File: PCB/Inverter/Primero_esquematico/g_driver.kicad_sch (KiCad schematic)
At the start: 31 parts, among them SW1 SW_Push, U14 SN74LVC1G08DCKR, U3 FS950R08A6P2BBPSA1

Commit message: Correcciones incompletas e instalaciones de un par de extensiones copadas
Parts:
- removed R29, R30, R31, R32, R33, R49, R50, R51, R52, R53, R69, R70, R71: 220k, symbol Device:R
- removed R34, R54: 6k8, symbol Device:R
- added R75, R76, R77, R84, R89, R90, R91, R93: 220k, symbol Device:R
- added R79: 6k8, symbol Device:R
- added TH1: ND03N00103K--, Capacitor_THT:C_Disc_D3.4mm_W2.1mm_P2.50mm, symbol Device:Thermistor_NTC
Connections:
- net GDsupply3/ISO_GND: now also R72.1, R74.2; no longer R74.1
- net GDsupply3/S_HV: now also R77.1; no longer R73.1, R74.2
- net GDsupply4/ISO_GND: now also TH1.1
- net GDsupply4/S_HV: now also TH1.2
- net GDsupply5/ISO_GND: now also R79.2, R84.1
- net GDsupply5/S_HV: now also R93.1
- net GND_DC: now also R74.1, R79.1
- new net: R89.1, R90.1
- new net: R84.2, R89.2
- new net: R73.1, R75.1
- new net: R90.2, R91.2
- new net: R75.2, R76.2
- new net: R76.1, R77.2
- new net: R91.1, R93.2
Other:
- removed sheet LogicSupply
- moved on the sheet: C67, C68, D84, D85, D86, R103, R104, R123, R124, R125, SW1, U14

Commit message: Termine el circuito de corriente
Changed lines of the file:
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@@
-	(wire
-		(pts
-			(xy 349.25 135.89) (xy 332.74 135.89)
-		)
-		(stroke
-			(width 0)
-			(type default)
-		)
-	)
 	(wire
 		(pts
@@
 	(wire
 		(pts
-			(xy 316.23 114.3) (xy 316.23 116.84)
-		)
-		(stroke
-			(width 0)
-			(type default)
-		)
-	)
-	(wire
-		(pts
 			(xy 223.52 144.78) (xy 226.06 144.78)
 		)
@@
 	(wire
 		(pts
-			(xy 332.74 135.89) (xy 332.74 114.3)
-		)
-		(stroke
-			(width 0)
-			(type default)
-		)
-	)
-	(wire
-		(pts
 			(xy 149.86 80.01) (xy 143.51 80.01)
 		)
@@
 	(wire
 		(pts
-			(xy 341.63 114.3) (xy 347.98 114.3)
-		)
-		(stroke
-			(width 0)
-			(type default)
-		)
-	)
-	(wire
-		(pts
 			(xy 207.01 93.98) (xy 199.39 93.98)
 		)
@@
 		)
 		(stroke
-			(width 0)
-			(type default)
-		)
-	)
-	(wire
-		(pts
-			(xy 332.74 114.3) (xy 334.01 114.3)
-		)
-		(stroke

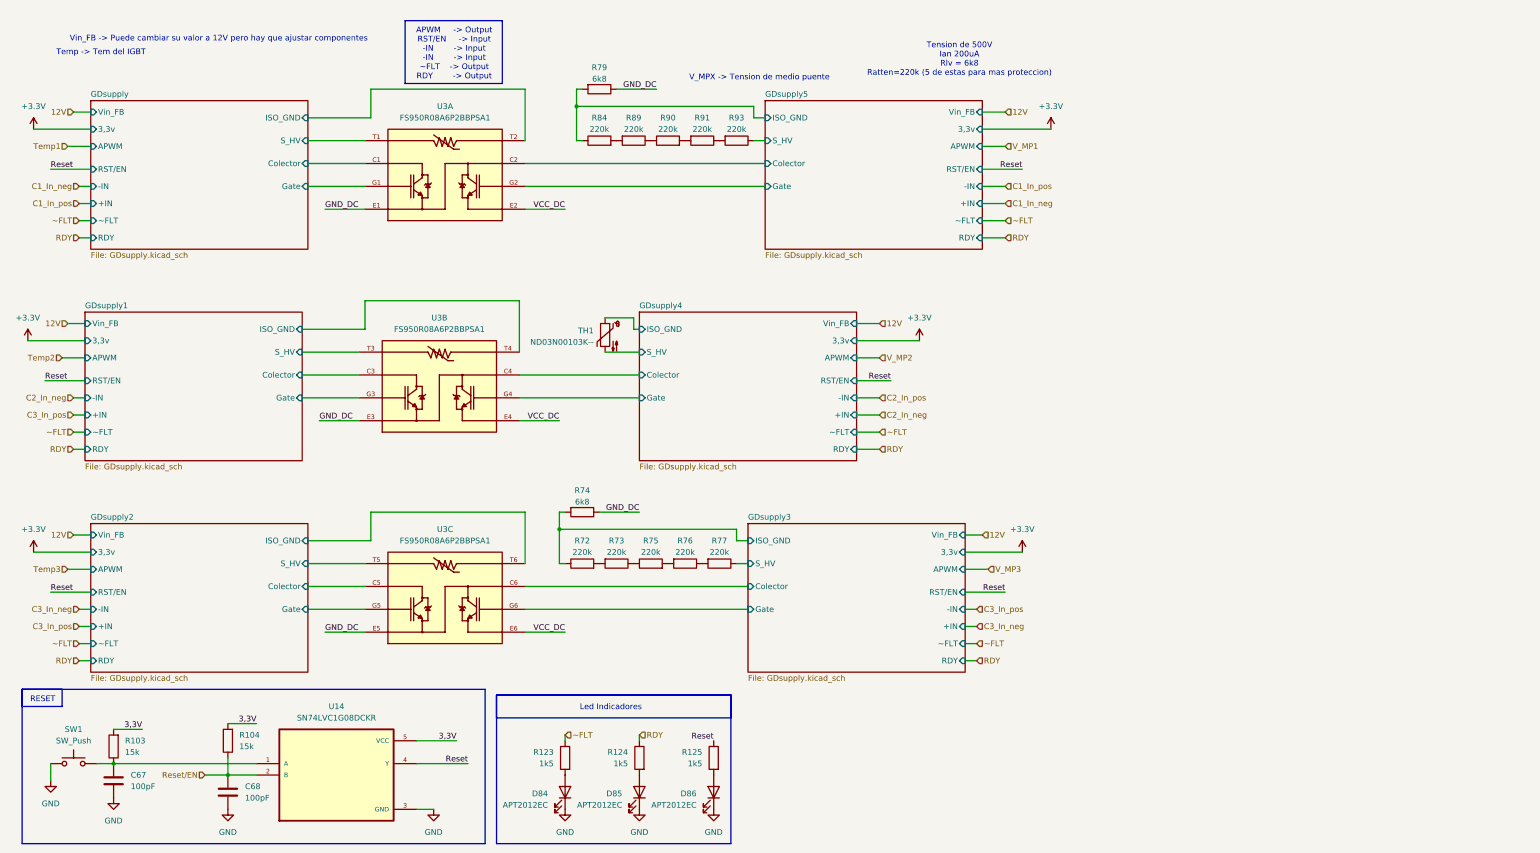
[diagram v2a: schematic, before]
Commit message: Coloque filtros y sensores
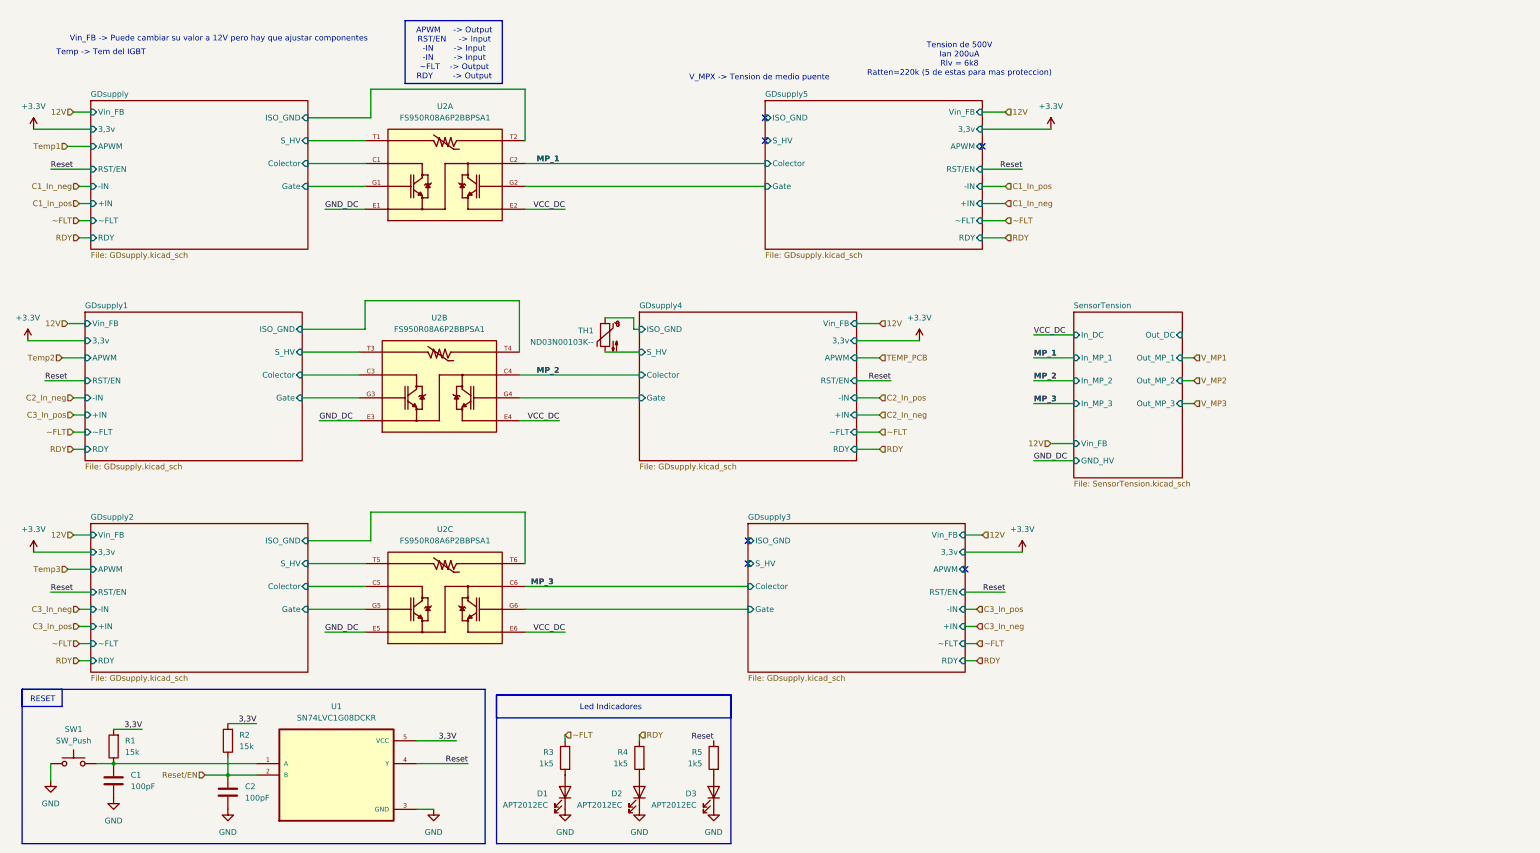
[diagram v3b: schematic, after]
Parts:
- removed R72, R73, R75, R76, R77, R84, R89, R90, R91, R93: 220k, symbol Device:R
- removed R74, R79: 6k8, symbol Device:R
- U1: renamed from U14; footprint SN74LVC1G08DCKR:SOT65P210X110-5N -> Snapeda:SOT65P210X110-5N
- U2: renamed from U3; footprint FSAE-footprints:IC_FS950R08A6P2BBPSA1 -> Snapeda:IC_FS950R08A6P2BBPSA1
- renumbered C67 to C1, C68 to C2, D84 to D1, D85 to D2, D86 to D3, R103 to R1, R104 to R2, R123 to R3, R124 to R4, R125 to R5
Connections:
- net GDsupply3/Colector renamed MP_3
- net GDsupply4/Colector renamed MP_2
- net GDsupply5/Colector renamed MP_1
- no-connect marks 0 -> 6
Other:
- added sheet SensorTension (SensorTension.kicad_sch)

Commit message: Esquematico practicamente terminado
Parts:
- removed C1, C2: 100pF, symbol Device:C
- removed R1, R2: 15k, symbol Device:R
- removed SW1: SW_Push, symbol Switch:SW_Push
- removed U1: SN74LVC1G08DCKR, Snapeda:SOT65P210X110-5N, symbol Fsae:SN74LVC1G08DCKR
- D1, D2, D3: footprint (none) -> LED_SMD:LED_0805_2012Metric
- R3, R4, R5: value 1k5 -> 2k2; footprint (none) -> Resistor_SMD:R_0603_1608Metric
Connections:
- net RDY: now also D2.2 (A)
- net Reset: no longer R5.1
- net Reset/EN: now also D3.2 (A), R5.1
- net ~FLT: now also D1.2 (A)
- net +3.3VA: now reaches R4.2
- net +3.3VA: now also R3.2, R5.2; no longer D2.2 (A)
- net GND renamed GND1
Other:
- note removed: "RESET"
- moved on the sheet: D1, D2, D3

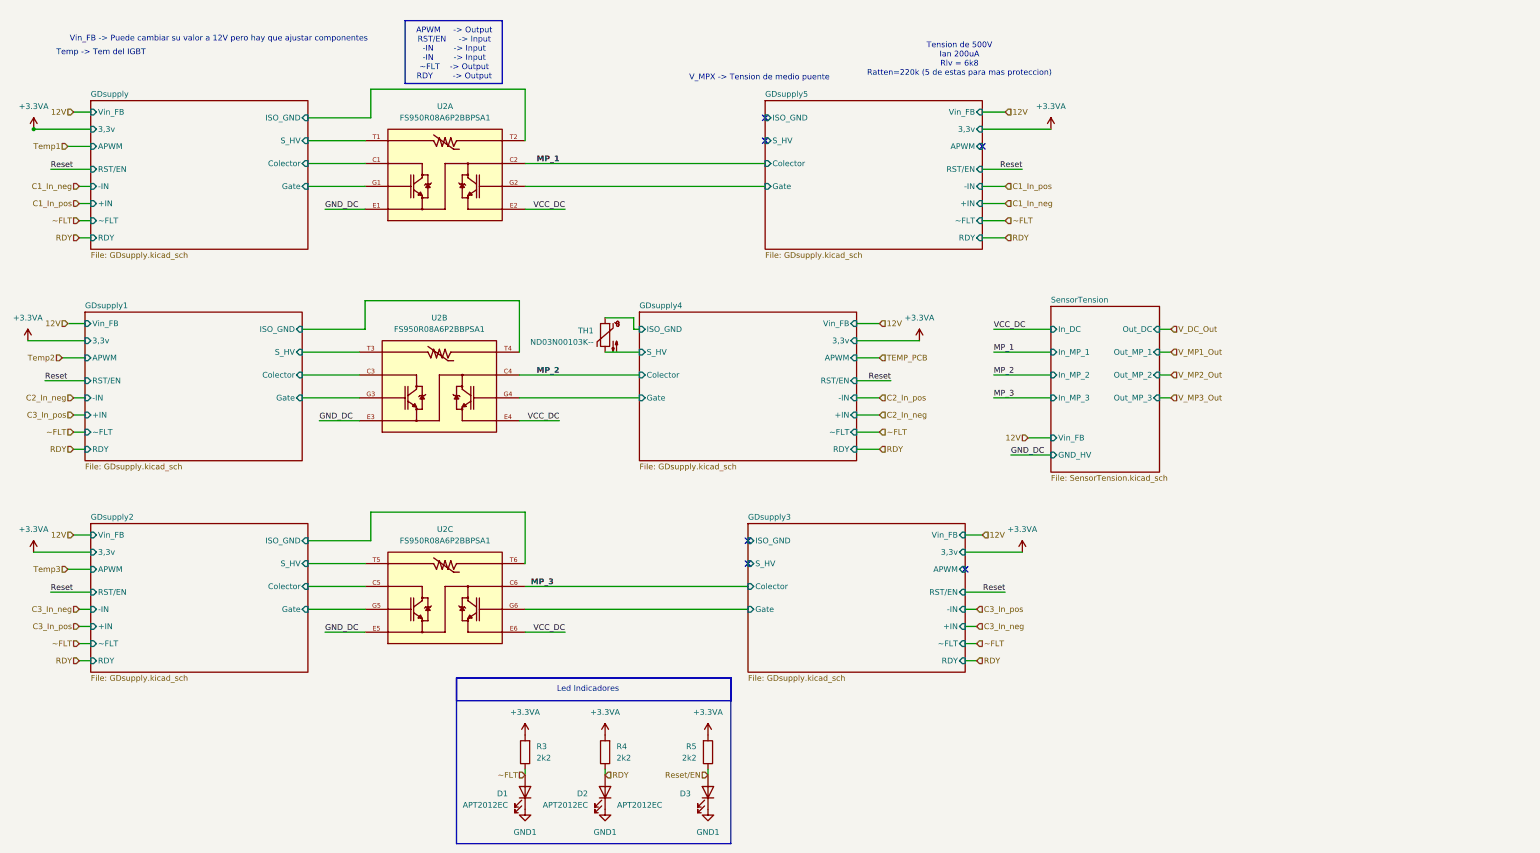
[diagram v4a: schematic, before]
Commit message: Un par de cosas q corregi del ERC pero sigue mal
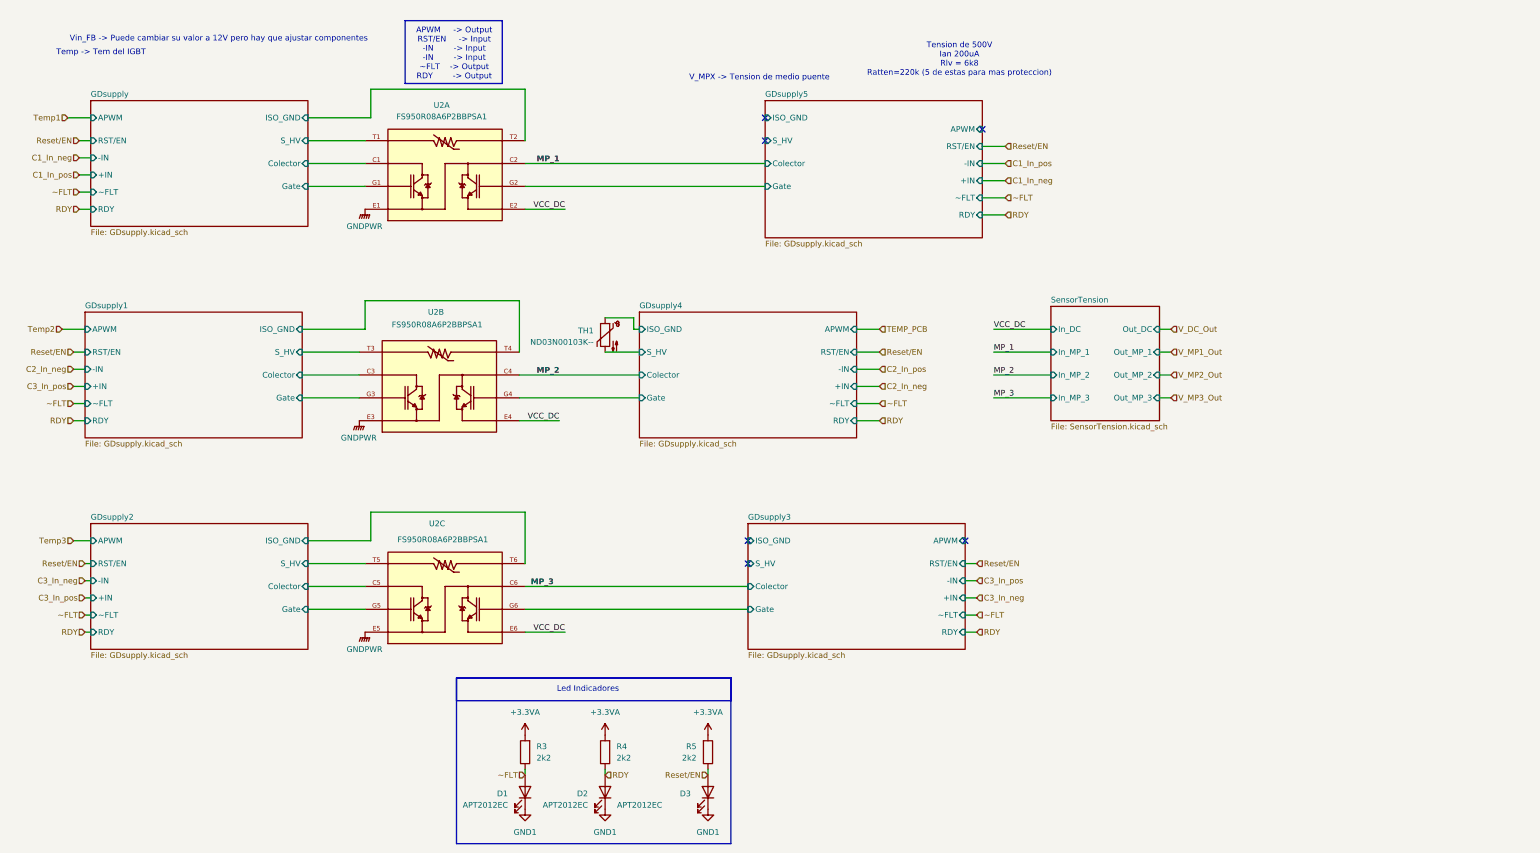
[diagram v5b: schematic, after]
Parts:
- removed U2: FS950R08A6P2BBPSA1, Snapeda:IC_FS950R08A6P2BBPSA1, symbol Fsae:FS950R08A6P2BBPSA1
- added U2: FS950R08A6P2BBPSA1, FS950R08A6P2BBPSA1:IC_FS950R08A6P2BBPSA1, symbol Snapeda:FS950R08A6P2BBPSA1
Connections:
- net GDsupply/Colector: now also U2.C1
- net GDsupply/Gate: now also U2.G1
- net GDsupply/ISO_GND: now also U2.T2
- net GDsupply/S_HV: now also U2.T1
- net GDsupply1/Colector: now also U2.C3
- net GDsupply1/Gate: now also U2.G3
- net GDsupply1/ISO_GND: now also U2.T4
- net GDsupply1/S_HV: now also U2.T3
- net GDsupply2/Colector: now also U2.C5
- net GDsupply2/Gate: now also U2.G5
- net GDsupply2/ISO_GND: now also U2.T6
- net GDsupply2/S_HV: now also U2.T5
- net GDsupply3/Gate: now also U2.G6
- net GDsupply4/Gate: now also U2.G4
- net GDsupply5/Gate: now also U2.G2
- net MP_1: now also U2.C2
- net MP_2: now also U2.C4
- net MP_3: now also U2.C6
- net VCC_DC: now also U2.E2, U2.E4, U2.E6
- new net GNDPWR: U2.E1, U2.E3, U2.E5
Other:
- sheet GDsupply ports: added none; removed 3,3v, Vin_FB
- sheet GDsupply1 ports: added none; removed 3,3v, Vin_FB
- sheet GDsupply2 ports: added none; removed 3,3v, Vin_FB
- sheet GDsupply3 ports: added none; removed 3,3v, Vin_FB
- sheet GDsupply4 ports: added none; removed 3,3v, Vin_FB
- sheet GDsupply5 ports: added none; removed 3,3v, Vin_FB
- sheet SensorTension ports: added none; removed GND_HV, Vin_FB

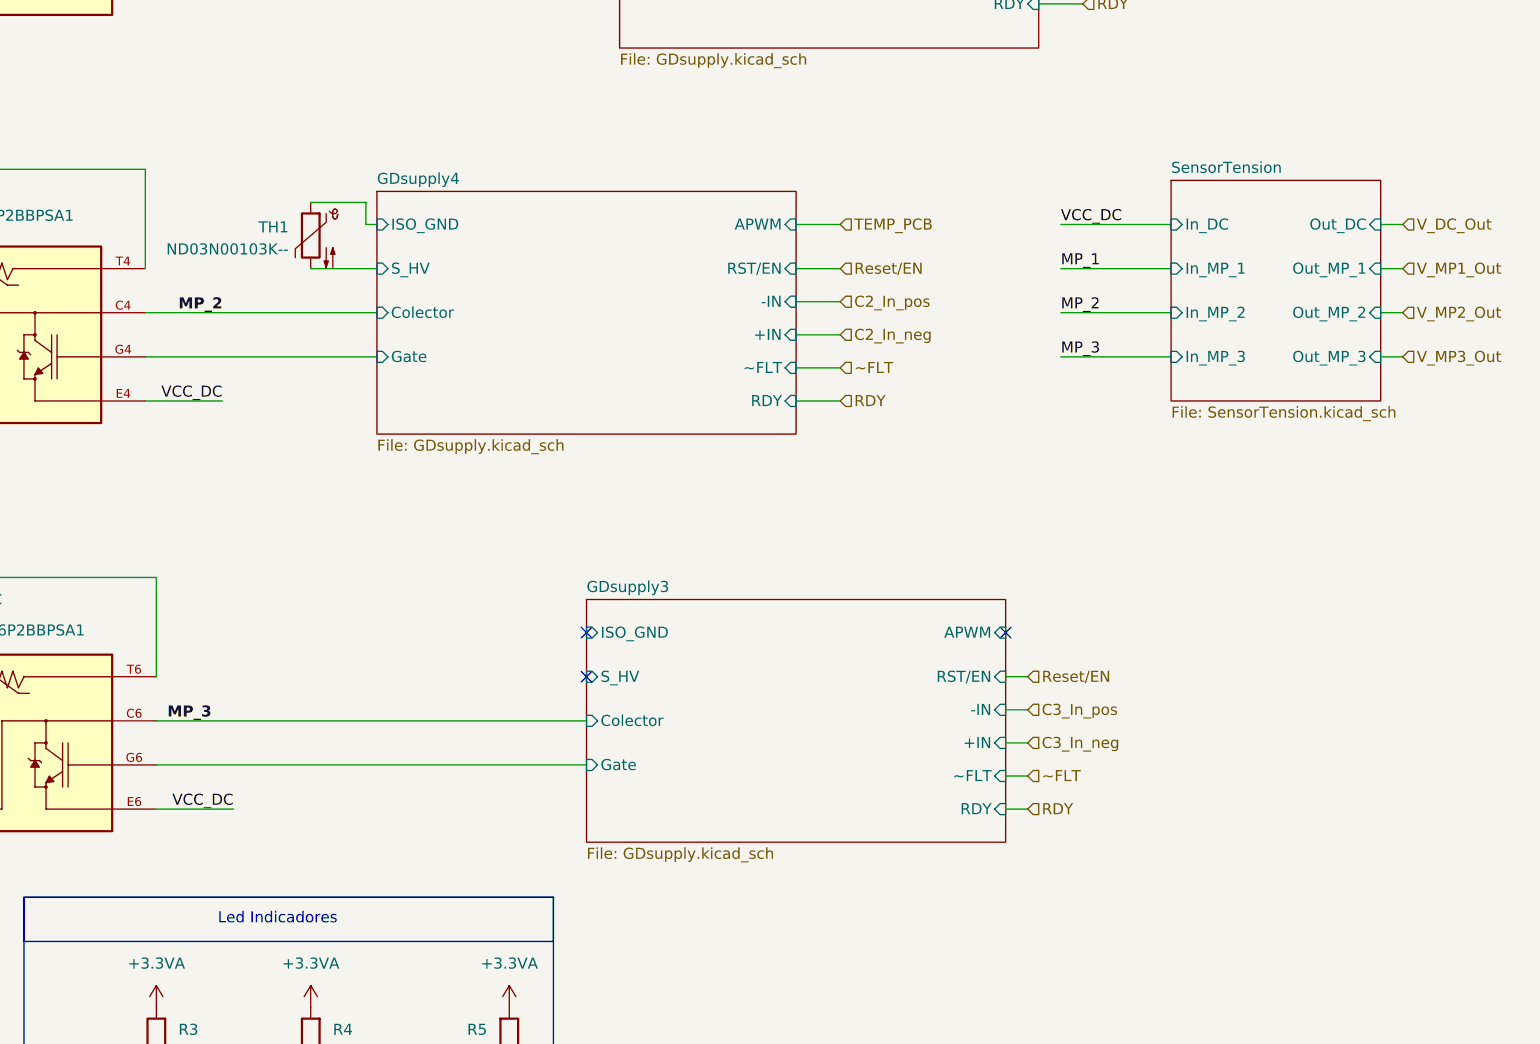
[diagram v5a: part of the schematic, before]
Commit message: Esquematico Listo
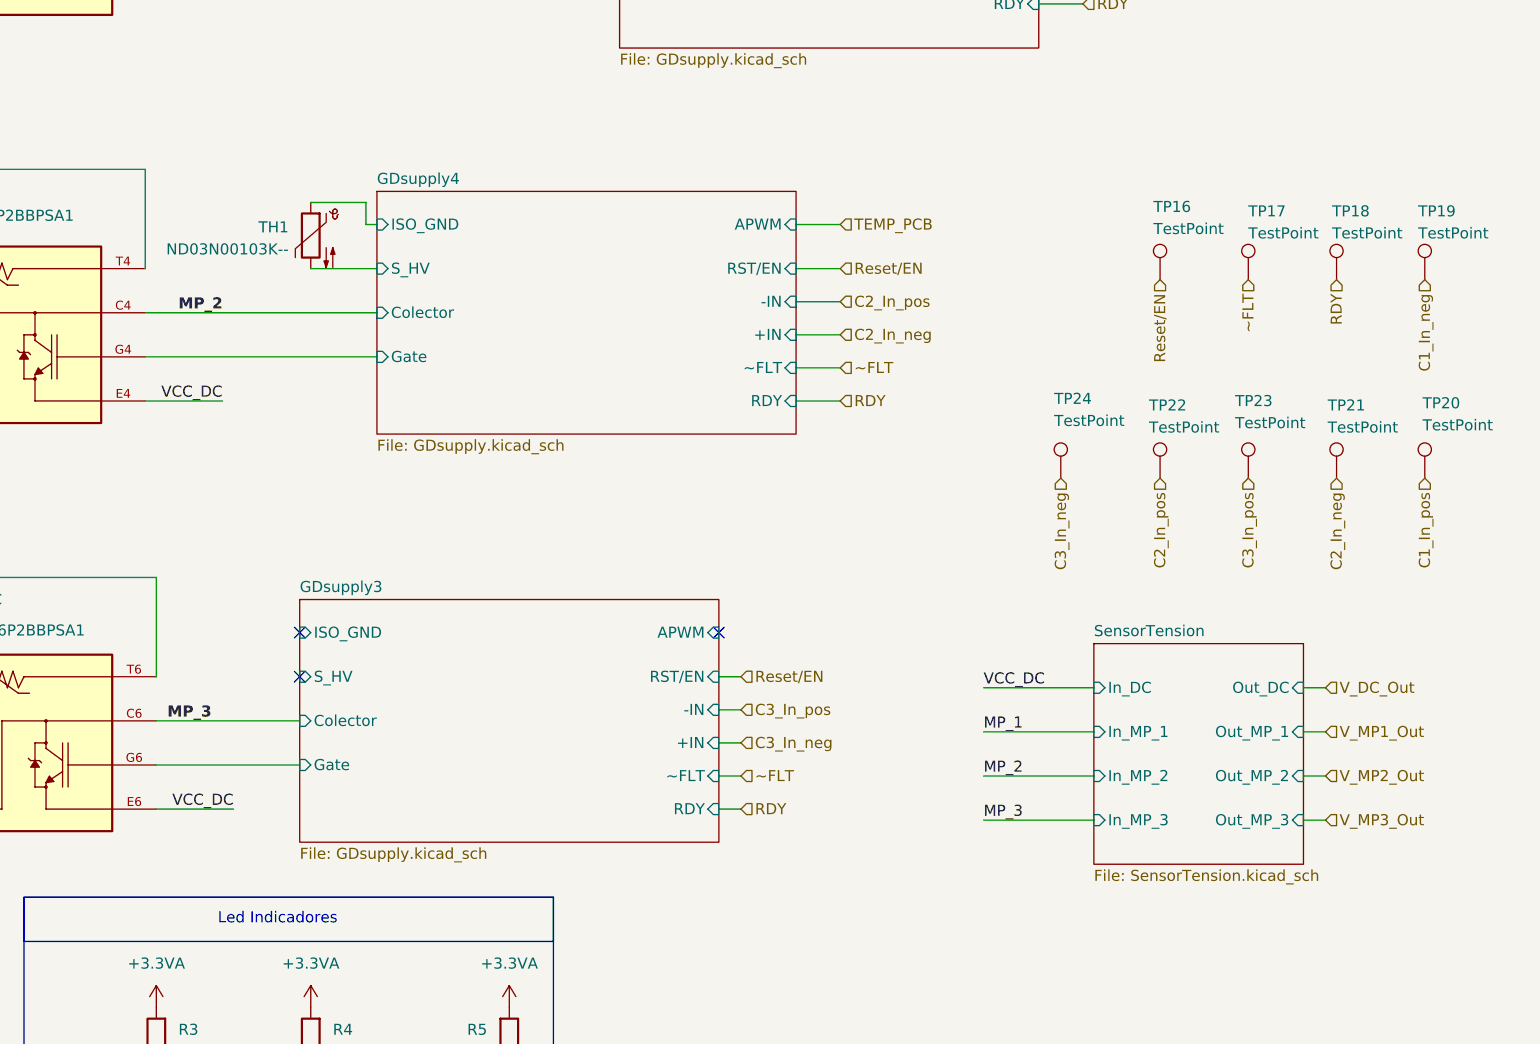
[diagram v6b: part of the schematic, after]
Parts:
- added TP16, TP17, TP18, TP19, TP20, TP21, TP22, TP23, TP24: TestPoint, TestPoint:TestPoint_Pad_D2.0mm, symbol Connector:TestPoint
- U2: footprint FS950R08A6P2BBPSA1:IC_FS950R08A6P2BBPSA1 -> Snapeda:IC_FS950R08A6P2BBPSA1
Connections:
- net C1_In_neg: now also TP19.1
- net C1_In_pos: now also TP20.1
- net C2_In_neg: now also TP21.1
- net C2_In_pos: now also TP22.1
- net C3_In_neg: now also TP24.1
- net C3_In_pos: now also TP23.1
- net RDY: now also TP18.1
- net Reset/EN: now also TP16.1
- net ~FLT: now also TP17.1
